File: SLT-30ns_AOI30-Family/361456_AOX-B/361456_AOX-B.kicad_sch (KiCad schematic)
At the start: 11 parts, among them U1 12-Pin_SLx_Can

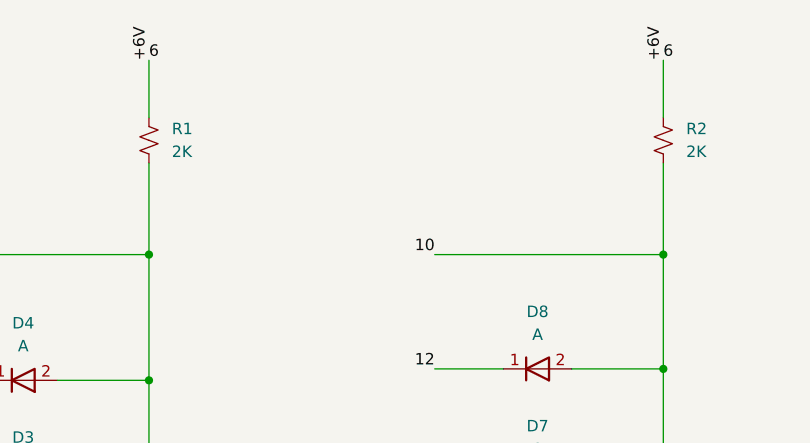
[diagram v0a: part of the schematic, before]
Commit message: Update schematic pdfs
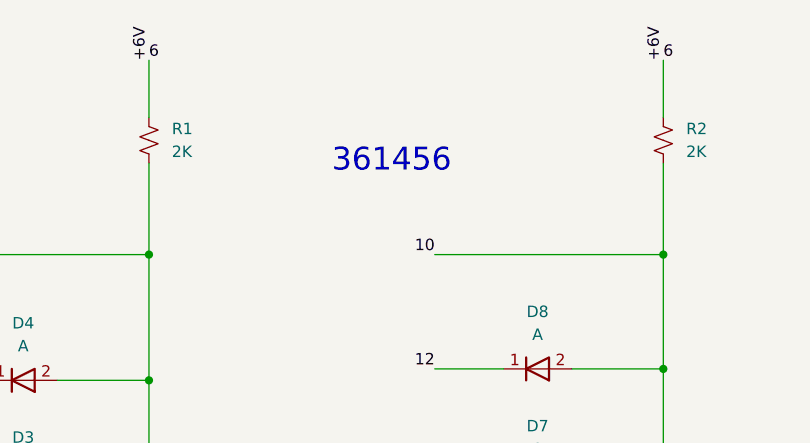
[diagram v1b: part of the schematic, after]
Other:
- note added: "361456"
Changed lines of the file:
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@@
     (stroke (width 0) (type default) (color 0 0 0 0))
+  )
+  (text "361456" (at 119.38 57.15 0)
+    (effects (font (size 2.54 2.54)) (justify left bottom))
   )
   (text "All Diodes \"A\"" (at 109.22 128.27 0)
